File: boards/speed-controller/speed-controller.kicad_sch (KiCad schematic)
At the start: 30 parts, among them J1 Screw_Terminal_01x02, J2 Screw_Terminal_01x02, J3 Screw_Terminal_01x02, Q1 BSS138, Q2 BSS138, SW1 SW_Push, U1 LM317_TO3, U2 LM317_TO3, U3 L298HN, U4 ESP32-WROOM-32D

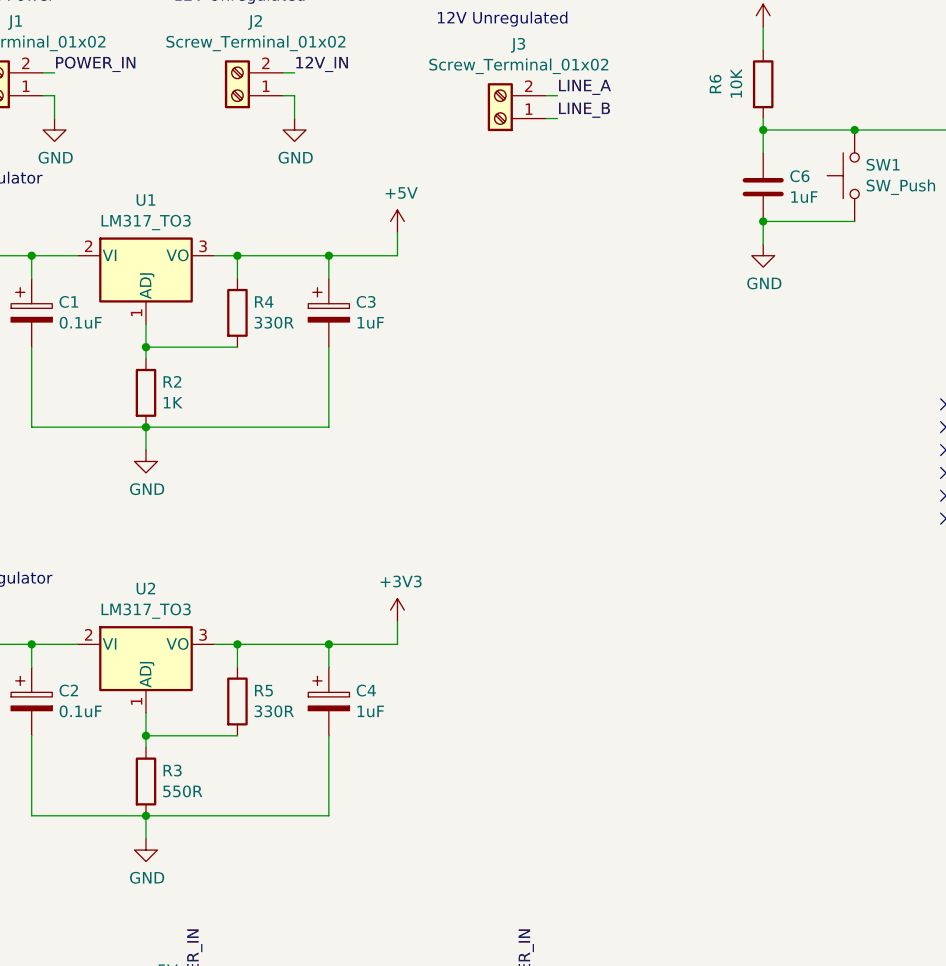
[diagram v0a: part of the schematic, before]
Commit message: Minor updates to values of components
Signed-off-by: Computroniks <mnickson@sidingsmedia.com>
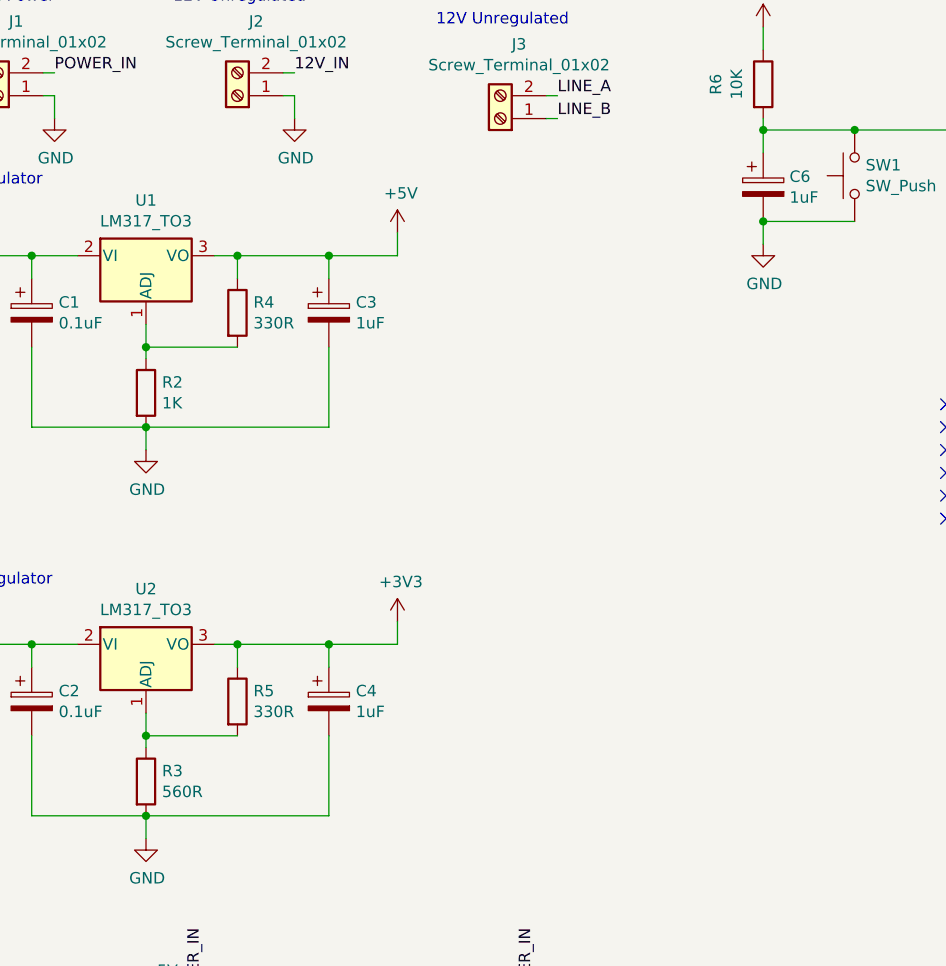
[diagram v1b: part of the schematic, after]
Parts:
- C6: symbol Device:C -> Device:C_Polarized
- R3: value 550R -> 560R
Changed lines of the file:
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@@
   (title_block
     (title "Speed Controller")
-    (date "2022-01-01")
-    (rev "1.0")
+    (date "2022-01-02")
+    (rev "1.0.1")
     (company "Matthew Nickson")
     (comment 1 "Licence: CC-BY-SA-4.0")
@@
       (effects (font (size 1.27 1.27)) (justify left))
     )
-    (property "Value" "550R" (id 1) (at 41.148 106.553 0)
+    (property "Value" "560R" (id 1) (at 41.148 106.553 0)
       (effects (font (size 1.27 1.27)) (justify left))
     )
@@
     (pin "1")
   )
-  (symbol (lib_id "Device:C") (at 107.95 39.37 0) (unit 1)
+  (symbol (lib_id "Device:C_Polarized") (at 107.95 39.37 0) (unit 1)
     (in_bom yes) (on_board yes)
     (property "Reference" "C6" (id 0) (at 110.871 38.2016 0)
@@
     )
     (path "/00000000-0000-0000-0000-000061d24e55"
-      (reference "R3") (unit 1) (value "550R") (footprint "Resistor_THT:R_Axial_DIN0207_L6.3mm_D2.5mm_P7.62mm_Horizontal")
+      (reference "R3") (unit 1) (value "560R") (footprint "Resistor_THT:R_Axial_DIN0207_L6.3mm_D2.5mm_P7.62mm_Horizontal")
     )
     (path "/00000000-0000-0000-0000-000061d1ba21"

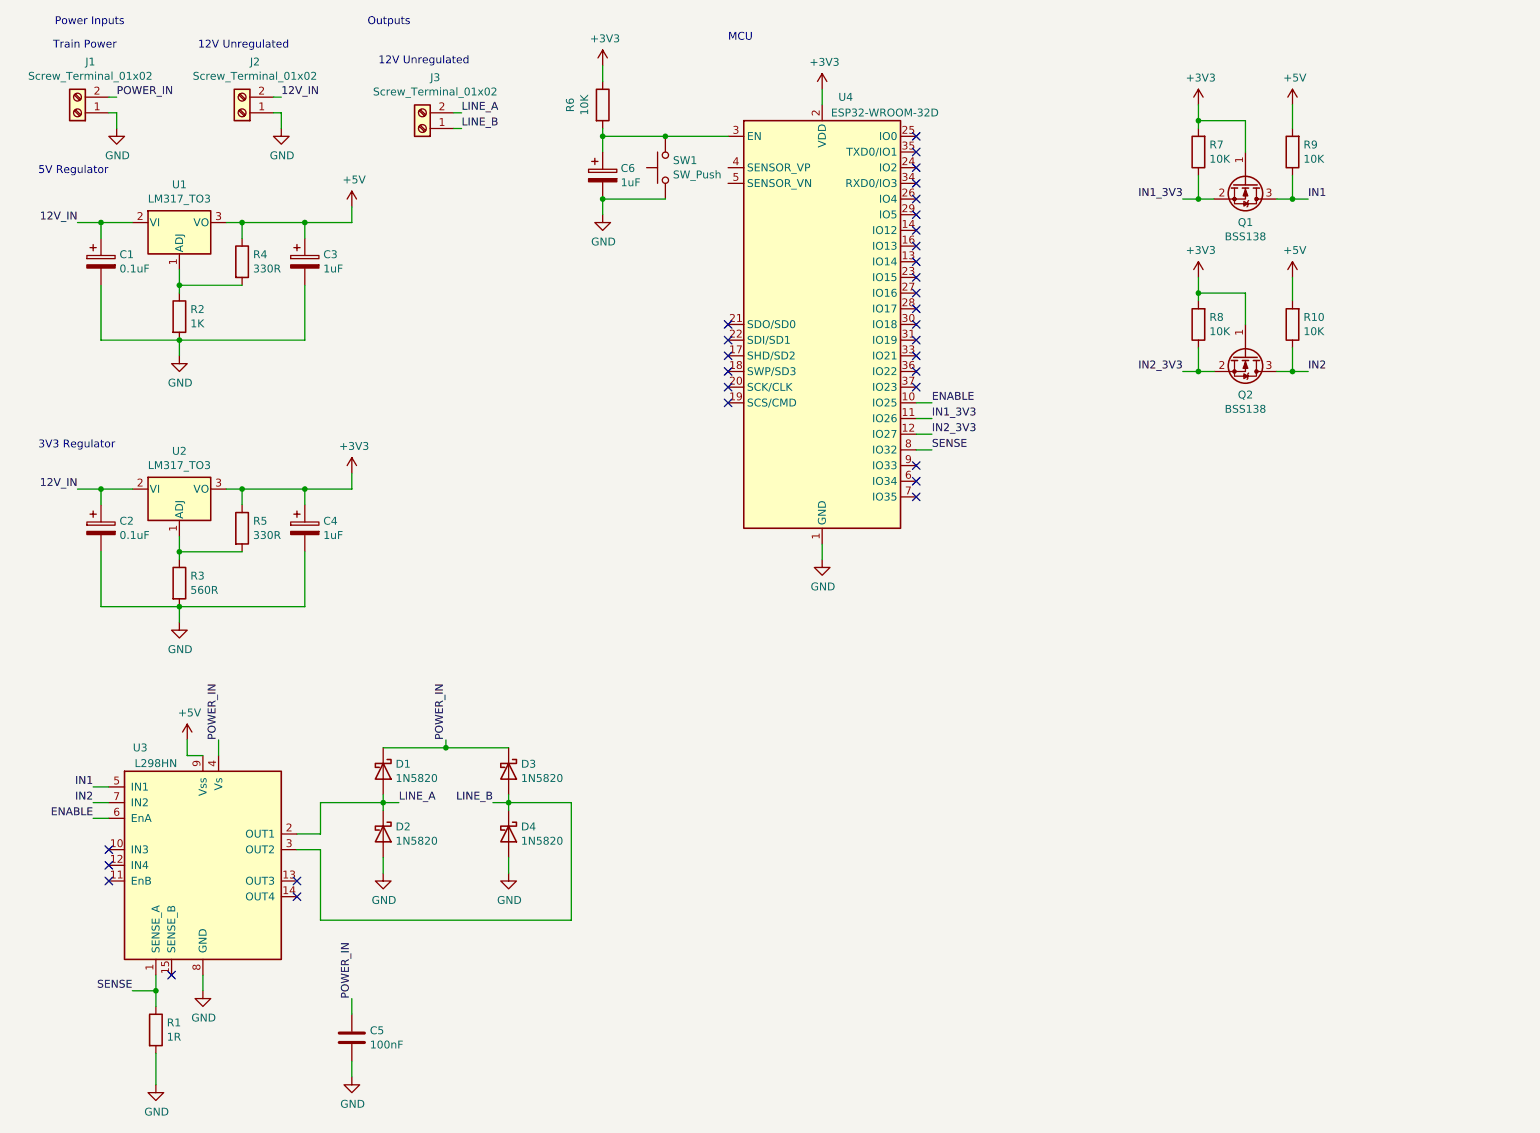
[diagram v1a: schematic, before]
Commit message: Added USB + assigned footprints
Signed-off-by: Computroniks <mnickson@sidingsmedia.com>
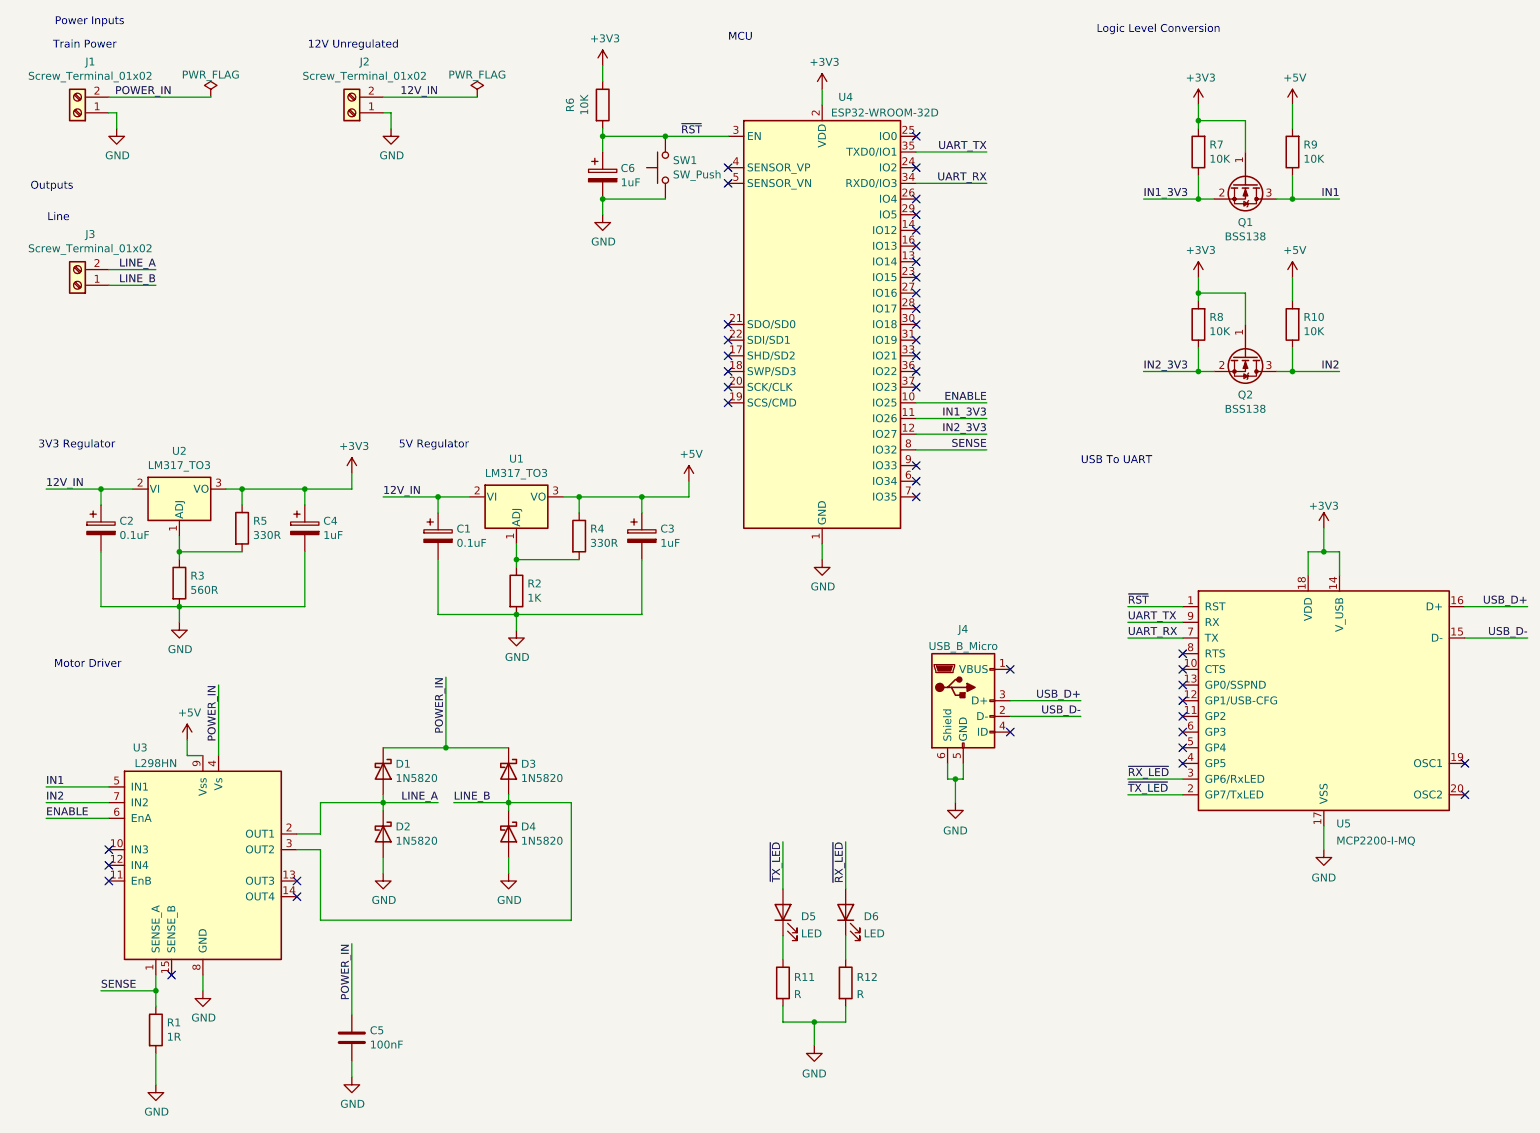
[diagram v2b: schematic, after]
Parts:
- added D5, D6: LED, LED_SMD:LED_0805_2012Metric, symbol Device:LED
- added J4: USB_B_Micro, Connector_USB:USB_Micro-B_Molex_47346-0001, symbol Connector:USB_B_Micro
- added R11, R12: R, Resistor_SMD:R_0805_2012Metric, symbol Device:R
- added U5: MCP2200-I-MQ, Package_DFN_QFN:QFN-20-1EP_5x5mm_P0.65mm_EP3.35x3.35mm, symbol Interface_USB:MCP2200-I-MQ
- C1, C2, C3, C4: footprint Capacitor_THT:CP_Radial_D5.0mm_P2.50mm -> Capacitor_SMD:CP_Elec_4x3
- C5: footprint Capacitor_THT:C_Disc_D6.0mm_W2.5mm_P5.00mm -> Capacitor_SMD:C_0805_2012Metric
- C6: footprint Capacitor_THT:CP_Radial_D5.0mm_P2.50mm -> Capacitor_SMD:C_0805_2012Metric
- D1, D2, D3, D4: footprint Diode_THT:D_DO-201AD_P15.24mm_Horizontal -> Diode_SMD:D_0805_2012Metric
- R1, R2: footprint Resistor_THT:R_Axial_DIN0922_L20.0mm_D9.0mm_P25.40mm_Horizontal -> Resistor_SMD:R_0805_2012Metric
- R10, R3, R4, R5, R6, R7, R8, R9: footprint Resistor_THT:R_Axial_DIN0207_L6.3mm_D2.5mm_P7.62mm_Horizontal -> Resistor_SMD:R_0805_2012Metric
- SW1: footprint Button_Switch_THT:SW_PUSH_6mm_H5mm -> Button_Switch_SMD:SW_Push_1P1T_NO_6x6mm_H9.5mm
- U1, U2: footprint Package_TO_SOT_THT:TO-220-3_Vertical -> Package_TO_SOT_SMD:SOT-223
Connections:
- net +3V3: now also U5.14 (V_USB), U5.18 (VDD)
- net GND: now also J4.5 (GND), J4.6 (Shield), R11.2, R12.2, U5.17 (VSS)
- net ~{RST}: now reaches C6.1, R6.2, SW1.2, U4.3 (EN)
- net ~{RST}: now also U5.1 (RST)
- net UART_RX: now reaches U4.34 (RXD0/IO3)
- net UART_RX: now also U5.7 (TX)
- net UART_TX: now reaches U4.35 (TXD0/IO1)
- net UART_TX: now also U5.9 (RX)
- new net: D6.1 (K), R12.1
- new net: D5.1 (K), R11.1
- new net USB_D+: J4.3 (D+), U5.16 (D+)
- new net USB_D-: J4.2 (D-), U5.15 (D-)
- new net ~{RX_LED}: D6.2 (A), U5.3 (GP6/RxLED)
- new net ~{TX_LED}: D5.2 (A), U5.2 (GP7/TxLED)
- no-connect marks 32 -> 44
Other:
- note added: "Line"
- note added: "Logic Level Conversion"
- note added: "Motor Driver"
- note added: "USB To UART"
- moved on the sheet: C1, C3, J2, J3, R2, R4, U1

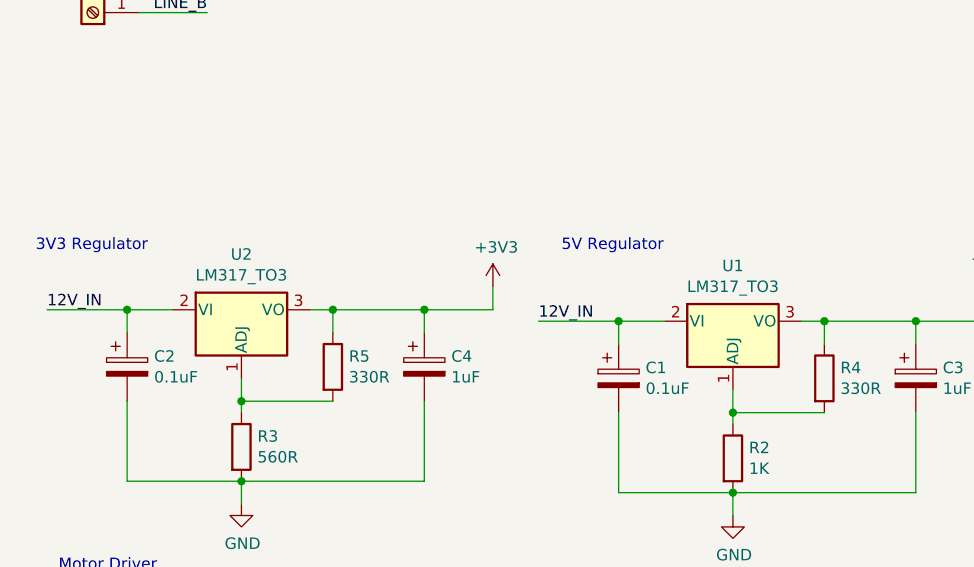
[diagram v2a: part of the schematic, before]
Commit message: Changed out LM317 + increment version
Signed-off-by: Computroniks <mnickson@sidingsmedia.com>
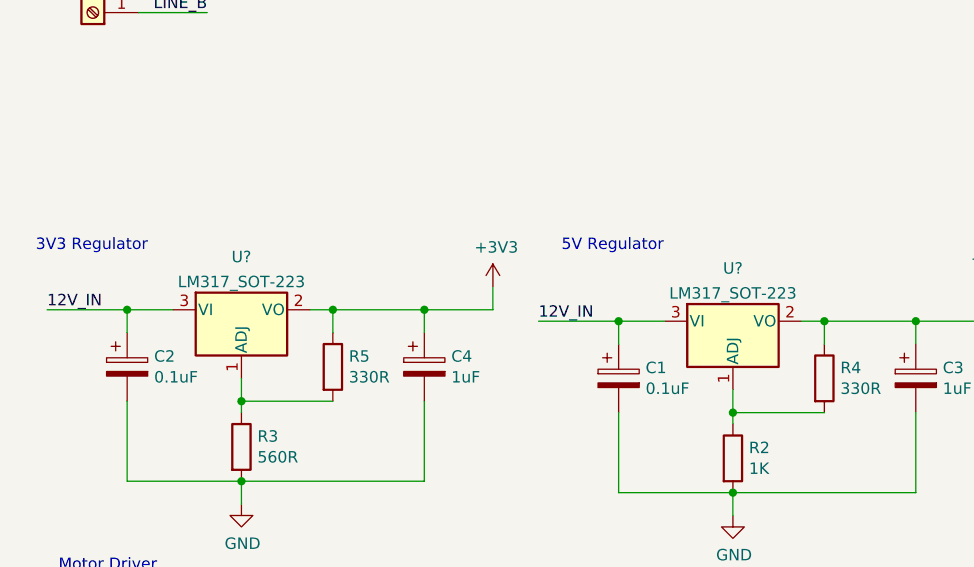
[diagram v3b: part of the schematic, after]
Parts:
- removed U1, U2: LM317_TO3, Package_TO_SOT_SMD:SOT-223, symbol Regulator_Linear:LM317_TO3
- added U? (x2): LM317_SOT-223, Package_TO_SOT_SMD:SOT-223-3_TabPin2, symbol Regulator_Linear:LM317_SOT-223
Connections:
- net +3V3: now also U?.2 (VO)
- net +5V: now also U?.2 (VO)
- net 12V_IN: now also U?.3 (VI), U?.3 (VI)
- net at R2.1, R4.2: now also U?.1 (ADJ)
- net at R3.1, R5.2: now also U?.1 (ADJ)
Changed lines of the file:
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@@
     (title "Speed Controller")
     (date "2022-03-19")
-    (rev "1.1.0")
+    (rev "V1.1.1")
     (company "Matthew Nickson")
     (comment 1 "Licence: CC-BY-SA-4.0")
@@
     (pin "1")
   )
-  (symbol (lib_id "Regulator_Linear:LM317_TO3") (at 93.98 91.44 0) (unit 1)
-    (in_bom yes) (on_board yes)
-    (property "Reference" "U1" (id 0) (at 93.98 85.2932 0))
-    (property "Value" "LM317_TO3" (id 1) (at 93.98 87.6046 0))
-    (property "Footprint" "Package_TO_SOT_SMD:SOT-223" (id 2) (at 93.98 86.36 0)
-      (effects (font (size 1.27 1.27) italic) hide)
-    )
-    (property "Datasheet" "http://www.ti.com/lit/ds/symlink/lm317.pdf" (id 3) (at 93.98 91.44 0)
-      (effects (font (size 1.27 1.27)) hide)
-    )
-    (pin "1")
-    (pin "2")
-    (pin "3")
-  )
   (symbol (lib_id "Device:CP") (at 81.28 97.79 0) (unit 1)
     (in_bom yes) (on_board yes)
@@
     (pin "9")
   )
-  (symbol (lib_id "Regulator_Linear:LM317_TO3") (at 39.37 90.17 0) (unit 1)
-    (in_bom yes) (on_board yes)
-    (property "Reference" "U2" (id 0) (at 39.37 84.0232 0))
-    (property "Value" "LM317_TO3" (id 1) (at 39.37 86.3346 0))
-    (property "Footprint" "Package_TO_SOT_SMD:SOT-223" (id 2) (at 39.37 85.09 0)
-      (effects (font (size 1.27 1.27) italic) hide)
-    )
-    (property "Datasheet" "http://www.ti.com/lit/ds/symlink/lm317.pdf" (id 3) (at 39.37 90.17 0)
-      (effects (font (size 1.27 1.27)) hide)
-    )
-    (pin "1")
-    (pin "2")
-    (pin "3")
-  )
   (symbol (lib_id "Device:CP") (at 26.67 96.52 0) (unit 1)
     (in_bom yes) (on_board yes)
@@
     (pin "6")
   )
+  (symbol (lib_id "Regulator_Linear:LM317_SOT-223") (at 93.98 91.44 0) (unit 1)
+    (in_bom yes) (on_board yes) (fields_autoplaced)
+    (property "Reference" "U?" (id 0) (at 93.98 85.5685 0))
+    (property "Value" "LM317_SOT-223" (id 1) (at 93.98 88.3436 0))
+    (property "Footprint" "Package_TO_SOT_SMD:SOT-223-3_TabPin2" (id 2) (at 93.98 85.09 0)
+      (effects (font (size 1.27 1.27) italic) hide)
+    )
+    (property "Datasheet" "http://www.ti.com/lit/ds/symlink/lm317.pdf" (id 3) (at 93.98 91.44 0)
+      (effects (font (size 1.27 1.27)) hide)
+    )
+    (pin "1")
+    (pin "2")
+    (pin "3")
+  )
   (symbol (lib_id "Device:R") (at 137.16 170.18 0) (unit 1)
     (in_bom yes) (on_board yes) (fields_autoplaced)
@@
     (pin "1")
   )
+  (symbol (lib_id "Regulator_Linear:LM317_SOT-223") (at 39.37 90.17 0) (unit 1)
+    (in_bom yes) (on_board yes) (fields_autoplaced)
+    (property "Reference" "U?" (id 0) (at 39.37 84.2985 0))
+    (property "Value" "LM317_SOT-223" (id 1) (at 39.37 87.0736 0))
+    (property "Footprint" "Package_TO_SOT_SMD:SOT-223-3_TabPin2" (id 2) (at 39.37 83.82 0)
+      (effects (font (size 1.27 1.27) italic) hide)
+    )
+    (property "Datasheet" "http://www.ti.com/lit/ds/symlink/lm317.pdf" (id 3) (at 39.37 90.17 0)
+      (effects (font (size 1.27 1.27)) hide)
+    )
+    (pin "1")
+    (pin "2")
+    (pin "3")
+  )
   (symbol (lib_id "power:GND") (at 142.24 180.34 0) (unit 1)
     (in_bom yes) (on_board yes) (fields_autoplaced)
@@
       (reference "SW1") (unit 1) (value "SW_Push") (footprint "Button_Switch_SMD:SW_Push_1P1T_NO_6x6mm_H9.5mm")
     )
-    (path "/00000000-0000-0000-0000-000061d1ba0a"
-      (reference "U1") (unit 1) (value "LM317_TO3") (footprint "Package_TO_SOT_SMD:SOT-223")
-    )
-    (path "/00000000-0000-0000-0000-000061d24e27"
-      (reference "U2") (unit 1) (value "LM317_TO3") (footprint "Package_TO_SOT_SMD:SOT-223")
-    )
     (path "/00000000-0000-0000-0000-000061d063aa"
       (reference "U3") (unit 1) (value "L298HN") (footprint "Package_TO_SOT_THT:TO-220-15_P2.54x2.54mm_StaggerOdd_Lead4.58mm_Vertical")
@@
       (reference "U5") (unit 1) (value "MCP2200-I-MQ") (footprint "Package_DFN_QFN:QFN-20-1EP_5x5mm_P0.65mm_EP3.35x3.35mm")
     )
-  )
+    (path "/7f0cc443-d897-4e16-abe0-1a89611d04cf"
+      (reference "U?") (unit 1) (value "LM317_SOT-223") (footprint "Package_TO_SOT_SMD:SOT-223-3_TabPin2")
+    )
+    (path "/e03bb906-5c6e-470d-a0a5-2488e1793551"
+      (reference "U?") (unit 1) (value "LM317_SOT-223") (footprint "Package_TO_SOT_SMD:SOT-223-3_TabPin2")
+    )
+  )
